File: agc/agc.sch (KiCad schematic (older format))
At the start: 62 parts, among them J5 SIL10, K1 SMD_HDR, K10 SMD_HDR, K11 SMD_HDR, K2 SMD_HDR, K3 SMD_HDR, K4 SMD_HDR, K5 SMD_HDR, K6 SMD_HDR, K7 SMD_HDR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

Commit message: component footprint changes to simplify bom
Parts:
- FID1, FID2, FID3: footprint (none) -> sdtransmitter:FID_1MM
- JP1, JP2, K1, K10, K11, K2, K3, K4, K5, K6, K7, K8, K9: footprint localconn:3-647166-3 -> sdtransmitter:0740991003
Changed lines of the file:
@@
 F 0 "K3" V 850 4550 50  0000 C CNN
 F 1 "SMD_HDR" V 950 4550 40  0000 C CNN
-F 2 "localconn:3-647166-3" H 900 4550 60  0001 C CNN
+F 2 "sdtransmitter:0740991003" H 900 4550 60  0001 C CNN
 F 3 "" H 900 4550 60  0000 C CNN
 	1    900  4550
@@
 F 0 "K5" V 12350 7850 50  0000 C CNN
 F 1 "SMD_HDR" V 12450 7850 40  0000 C CNN
-F 2 "localconn:3-647166-3" H 12400 7850 60  0001 C CNN
+F 2 "sdtransmitter:0740991003" H 12400 7850 60  0001 C CNN
 F 3 "" H 12400 7850 60  0000 C CNN
 	1    12400 7850
@@
 F 0 "K1" V 12350 7400 50  0000 C CNN
 F 1 "SMD_HDR" V 12450 7400 40  0000 C CNN
-F 2 "localconn:3-647166-3" H 12400 7400 60  0001 C CNN
+F 2 "sdtransmitter:0740991003" H 12400 7400 60  0001 C CNN
 F 3 "" H 12400 7400 60  0000 C CNN
 	1    12400 7400
@@
 F 0 "K7" V 10300 3450 50  0000 C CNN
 F 1 "SMD_HDR" V 10400 3450 40  0000 C CNN
-F 2 "localconn:3-647166-3" H 10350 3450 60  0001 C CNN
+F 2 "sdtransmitter:0740991003" H 10350 3450 60  0001 C CNN
 F 3 "" H 10350 3450 60  0000 C CNN
 	1    10350 3450
@@
 F 0 "JP2" H 14150 3200 60  0000 C CNN
 F 1 "SMD_HDR" H 14150 2970 40  0000 C CNN
-F 2 "localconn:3-647166-3" H 14150 3050 60  0001 C CNN
+F 2 "sdtransmitter:0740991003" H 14150 3050 60  0001 C CNN
 F 3 "" H 14150 3050 60  0000 C CNN
 	1    14150 3050
@@
 F 0 "K2" V 12350 8400 50  0000 C CNN
 F 1 "SMD_HDR" V 12450 8400 40  0000 C CNN
-F 2 "localconn:3-647166-3" H 12400 8400 60  0001 C CNN
+F 2 "sdtransmitter:0740991003" H 12400 8400 60  0001 C CNN
 F 3 "" H 12400 8400 60  0000 C CNN
 	1    12400 8400
@@
 F 0 "K4" V 850 3300 50  0000 C CNN
 F 1 "SMD_HDR" V 950 3300 40  0000 C CNN
-F 2 "localconn:3-647166-3" H 900 3300 60  0001 C CNN
+F 2 "sdtransmitter:0740991003" H 900 3300 60  0001 C CNN
 F 3 "" H 900 3300 60  0000 C CNN
 	1    900  3300
@@
 F 0 "K6" V 12350 9050 50  0000 C CNN
 F 1 "SMD_HDR" V 12450 9050 40  0000 C CNN
-F 2 "localconn:3-647166-3" H 12400 9050 60  0001 C CNN
+F 2 "sdtransmitter:0740991003" H 12400 9050 60  0001 C CNN
 F 3 "" H 12400 9050 60  0000 C CNN
 	1    12400 9050
@@
 F 0 "K8" V 15050 7800 50  0000 C CNN
 F 1 "SMD_HDR" V 15150 7800 40  0000 C CNN
-F 2 "localconn:3-647166-3" H 15100 7800 60  0001 C CNN
+F 2 "sdtransmitter:0740991003" H 15100 7800 60  0001 C CNN
 F 3 "" H 15100 7800 60  0000 C CNN
 	1    15100 7800
@@
 F 0 "K9" V 15050 8250 50  0000 C CNN
 F 1 "SMD_HDR" V 15150 8250 40  0000 C CNN
-F 2 "localconn:3-647166-3" H 15100 8250 60  0001 C CNN
+F 2 "sdtransmitter:0740991003" H 15100 8250 60  0001 C CNN
 F 3 "" H 15100 8250 60  0000 C CNN
 	1    15100 8250
@@
 F 0 "JP1" H 8100 2050 60  0000 C CNN
 F 1 "SMD_HDR" H 8100 1820 40  0000 C CNN
-F 2 "localconn:3-647166-3" H 8100 1900 60  0001 C CNN
+F 2 "sdtransmitter:0740991003" H 8100 1900 60  0001 C CNN
 F 3 "" H 8100 1900 60  0000 C CNN
 	1    8100 1900
@@
 F 0 "K10" V 7200 3900 50  0000 C CNN
 F 1 "SMD_HDR" V 7300 3900 40  0000 C CNN
-F 2 "localconn:3-647166-3" H 7250 3900 60  0001 C CNN
+F 2 "sdtransmitter:0740991003" H 7250 3900 60  0001 C CNN
 F 3 "" H 7250 3900 60  0000 C CNN
 	1    7250 3900
@@
 F 0 "K11" V 13250 6650 50  0000 C CNN
 F 1 "SMD_HDR" V 13350 6650 40  0000 C CNN
-F 2 "localconn:3-647166-3" H 13300 6650 60  0001 C CNN
+F 2 "sdtransmitter:0740991003" H 13300 6650 60  0001 C CNN
 F 3 "" H 13300 6650 60  0000 C CNN
 	1    13300 6650
@@
 F 0 "FID1" H 4300 4600 60  0000 C CNN
 F 1 "FIDUCIAL MARKER" H 4600 4700 60  0000 C CNN
-F 2 "" H 4600 4550 60  0000 C CNN
+F 2 "sdtransmitter:FID_1MM" H 4600 4550 60  0001 C CNN
 F 3 "" H 4600 4550 60  0000 C CNN
 	1    4600 4550
@@
 F 0 "FID2" H 5150 4600 60  0000 C CNN
 F 1 "FIDUCIAL MARKER" H 5450 4700 60  0000 C CNN
-F 2 "" H 5450 4550 60  0000 C CNN
+F 2 "sdtransmitter:FID_1MM" H 5450 4550 60  0001 C CNN
 F 3 "" H 5450 4550 60  0000 C CNN
 	1    5450 4550
@@
 F 0 "FID3" H 4300 4900 60  0000 C CNN
 F 1 "FIDUCIAL MARKER" H 4600 5000 60  0000 C CNN
-F 2 "" H 4600 4850 60  0000 C CNN
+F 2 "sdtransmitter:FID_1MM" H 4600 4850 60  0001 C CNN
 F 3 "" H 4600 4850 60  0000 C CNN
 	1    4600 4850

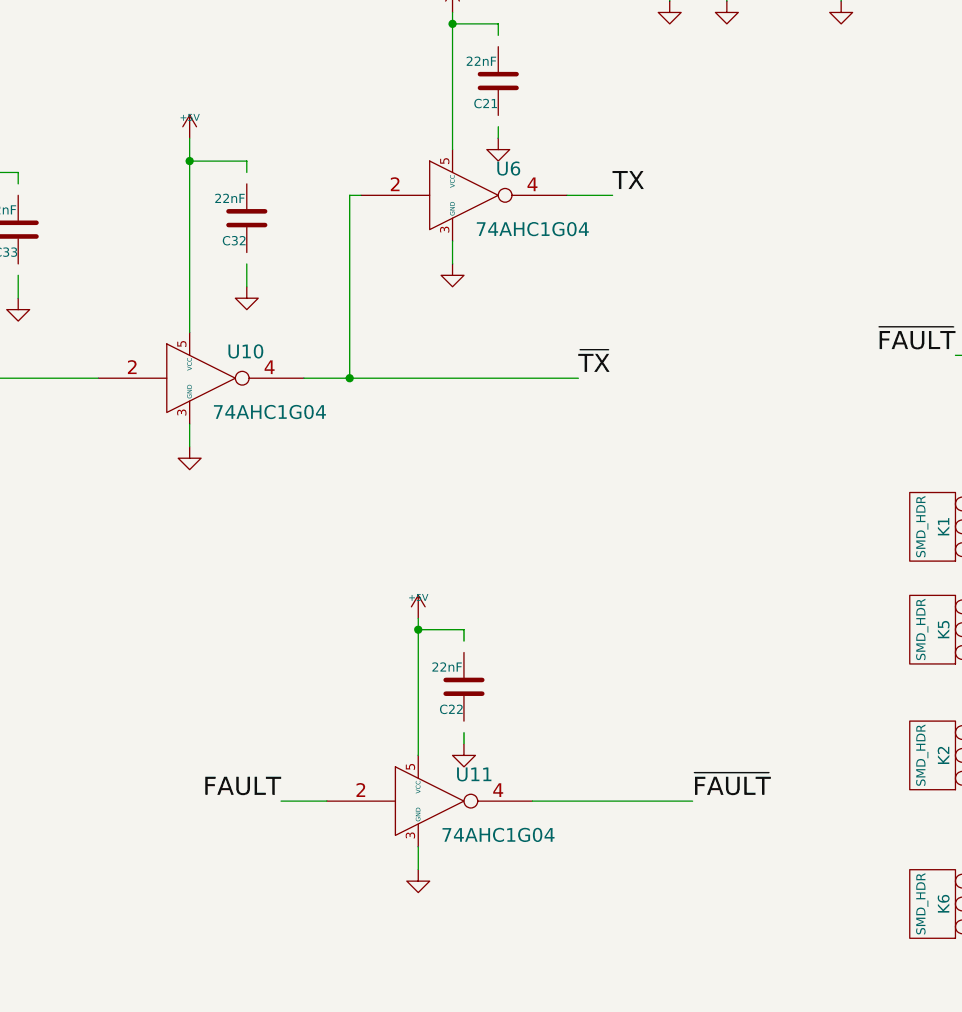
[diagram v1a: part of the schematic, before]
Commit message: added digikey bom for driver amplifier production run
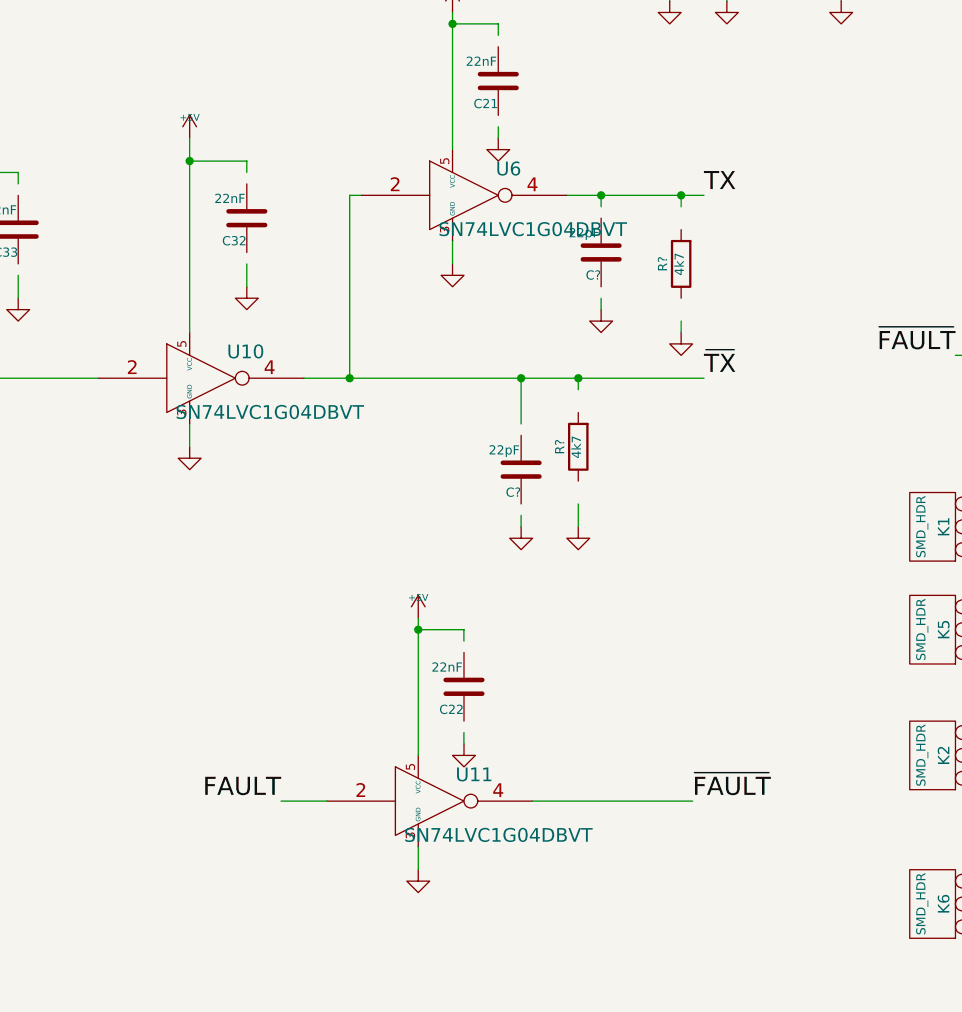
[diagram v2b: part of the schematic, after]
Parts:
- added C? (x2): 22pF, SMD_Packages:SMD-0805, symbol C
- added R? (x2): 4k7, SMD_Packages:SMD-0805, symbol R
- U10, U11, U6: value 74AHC1G04 -> SN74LVC1G04DBVT
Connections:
- wire segments 192 -> 200

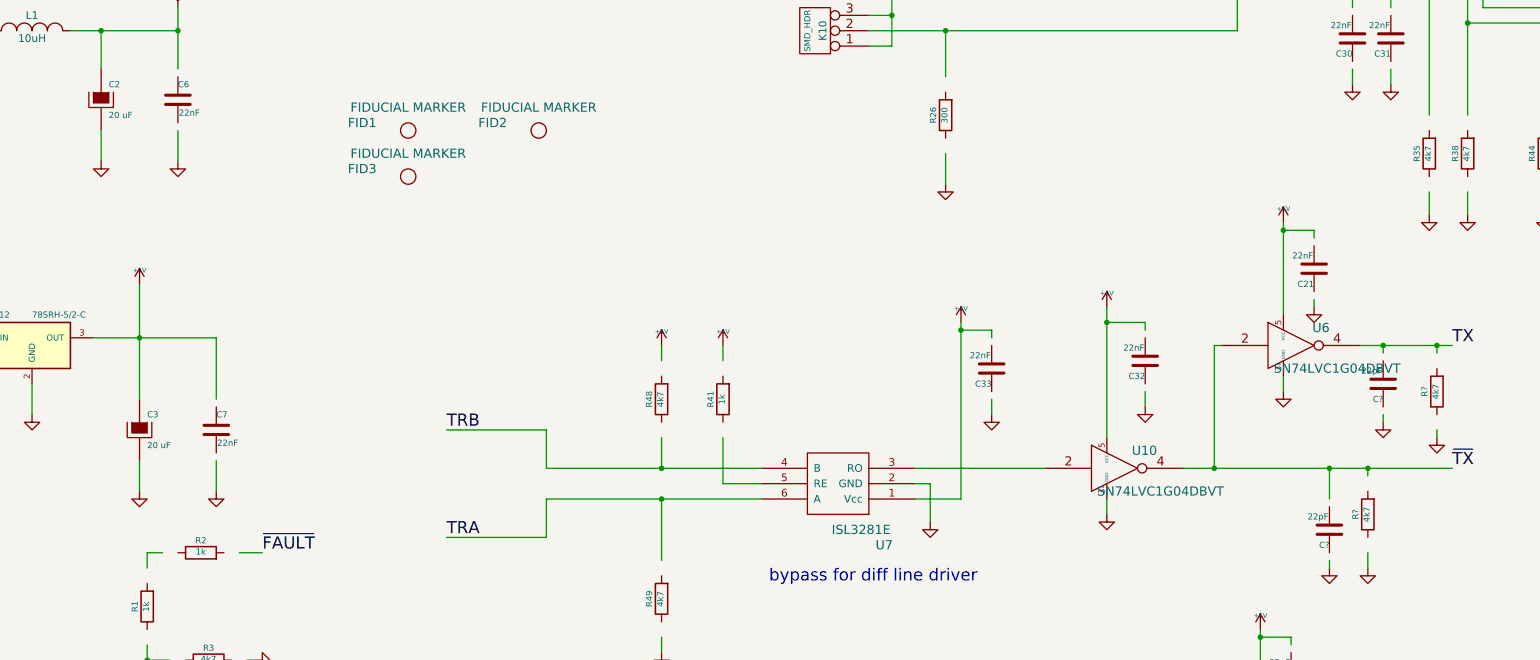
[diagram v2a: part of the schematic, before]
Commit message: added digikey bom for control
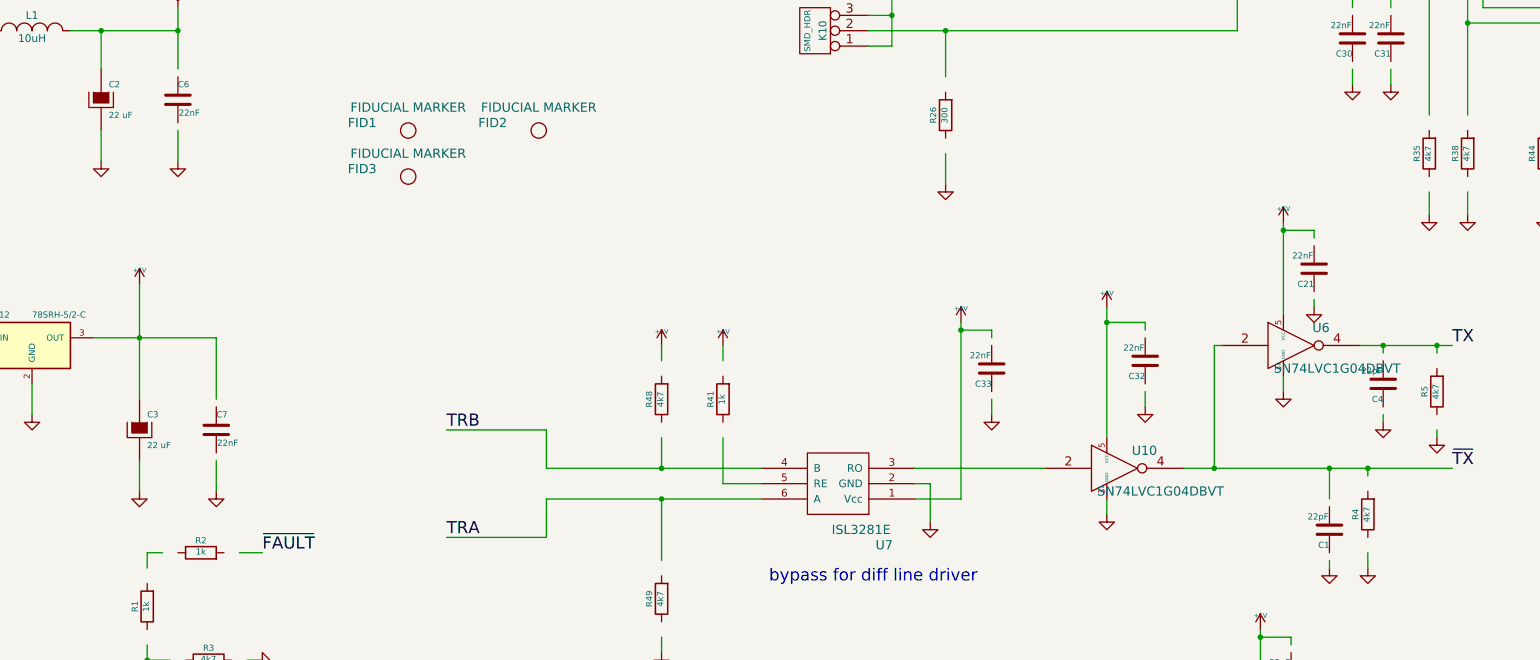
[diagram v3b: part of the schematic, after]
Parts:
- C2, C3: value 20 uF -> 22 uF
- gave numbers to parts that had none: 4

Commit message: added fields for manufacturer/distributor part number to schematic
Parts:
- C1, C4: Dist Name (none) -> DigiKey; Dist PN (none) -> 1276-2607-6-ND; MFG Name (none) -> SAMSUNG ELECTRO-MECHANICS AMERICA, INC (VA); MFG PN (none) -> CL21C220JCANNNC
- C2: Dist Name (none) -> DigiKey; Dist PN (none) -> TDK CORPORATION (VA); MFG Name (none) -> 445-3955-6-ND; MFG PN (none) -> C3225X7R1C226M250AC
- C21: Dist Name (none) -> DigiKey; MFG Name (none) -> MURATA ELECTRONICS (VA); MFG PN (none) -> GRM21BR72A223KA01L
- C22, C28, C29, C30, C31, C32, C33, C6, C7: Dist Name (none) -> DigiKey; Dist PN (none) -> 490-1658-6-ND; MFG Name (none) -> MURATA ELECTRONICS (VA); MFG PN (none) -> GRM21BR72A223KA01L
- C3: Dist Name (none) -> DigiKey; MFG Name (none) -> 445-3955-6-ND; MFG PN (none) -> C3225X7R1C226M250AC
- J5: Dist Name (none) -> DigiKey; Dist PN (none) -> 4610X-1-103LF-ND; MFG Name (none) -> BOURNS INC; MFG PN (none) -> 4610X-101-103LF
- JP1, JP2, K1, K10, K11, K2, K3, K5, K6, K7, K8, K9: Dist Name (none) -> DigiKey; Dist PN (none) -> WM7203-ND; MFG Name (none) -> MOLEX INC; MFG PN (none) -> 740991003
- K4: Dist Name (none) -> Digikey; Dist PN (none) -> WM7203-ND; MFG Name (none) -> MOLEX INC; MFG PN (none) -> 740991003
- L1: Dist Name (none) -> DigiKey; Dist PN (none) -> 587-2409-6-ND; MFG Name (none) -> TAIYO YUDEN (VA); MFG PN (none) -> NRS5020T100MMGJ
- P4: Dist Name (none) -> DigiKey; Dist PN (none) -> 3M11931-ND; MFG Name (none) -> 3M; MFG PN (none) -> 30316-6002HB
- R1, R2, R34, R37, R41, R43: Dist Name (none) -> DigiKey; Dist PN (none) -> P1.00KCDKR-ND; MFG Name (none) -> PANASONIC ELECTRONIC COMPONENTS (VA); MFG PN (none) -> ERJ-6ENF1001V
- R18, R3, R35, R38, R4, R44, R45, R48, R49, R5: Dist Name (none) -> DigiKey; Dist PN (none) -> P4.70KCDKR-ND; MFG Name (none) -> PANASONIC ELECTRONIC COMPONENTS (VA); MFG PN (none) -> ERJ-6ENF4701V
- R23, R33, R36: Dist Name (none) -> DigiKey; Dist PN (none) -> P20.0KCDKR-ND; MFG Name (none) -> PANASONIC ELECTRONIC COMPONENTS (VA); MFG PN (none) -> ERJ-6ENF2002V
- R25, R26: Dist Name (none) -> DigiKey; Dist PN (none) -> P300CDKR-ND; MFG Name (none) -> PANASONIC ELECTRONIC COMPONENTS (VA); MFG PN (none) -> ERJ-6ENF3000V
- R42: Dist Name (none) -> DigiKey; Dist PN (none) -> P100KCDKR-ND; MFG Name (none) -> PANASONIC ELECTRONIC COMPONENTS (VA); MFG PN (none) -> ERJ-6ENF1003V
- U10, U11, U6: Dist Name (none) -> DigiKey; Dist PN (none) -> 296-32289-6-ND; MFG Name (none) -> TEXAS INSTRUMENTS (VA); MFG PN (none) -> SN74LVC1G04DBVT
- U12: Dist Name (none) -> DigiKey; Dist PN (none) -> 811-1119-ND; MFG Name (none) -> MURATA POWER SOLUTIONS INC; MFG PN (none) -> 78SR-5/2-C
- U7: Dist Name (none) -> DigiKey; Dist PN (none) -> ISL3281EIHZ-TDKR-ND; MFG Name (none) -> INTERSIL (VA); MFG PN (none) -> ISL3281EIHZ-T
- U9: Dist Name (none) -> DigiKey; Dist PN (none) -> ADM2914-2ARQZ-ND; MFG Name (none) -> ANALOG DEVICES INC; MFG PN (none) -> ADM2914-2ARQZ

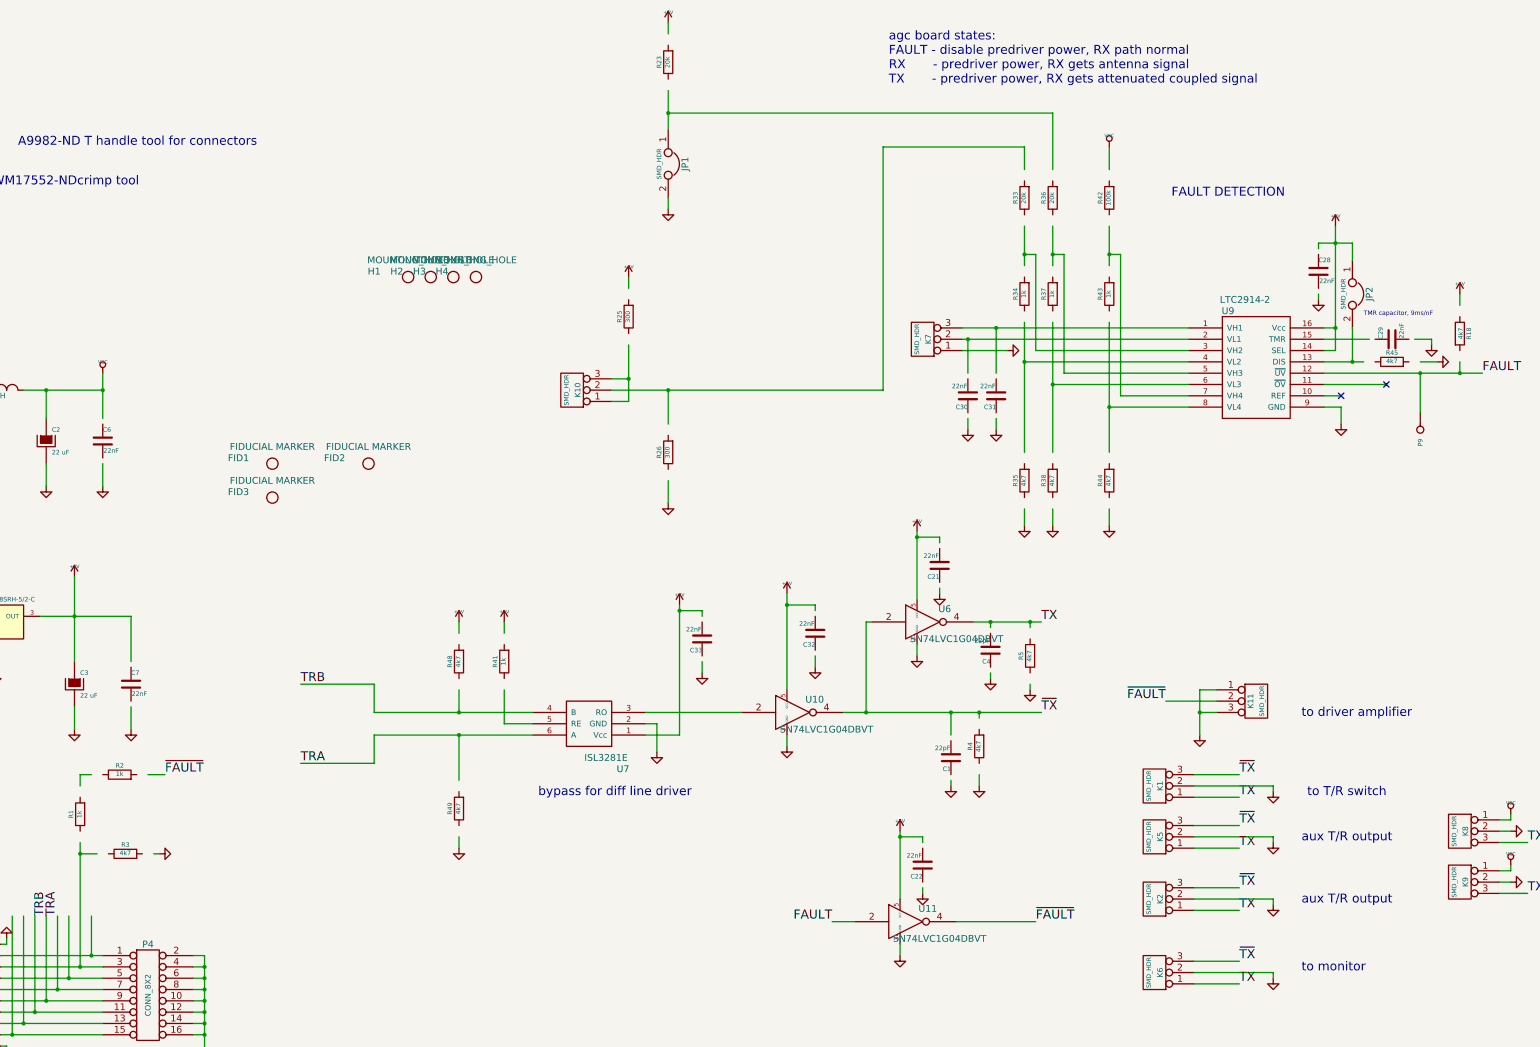
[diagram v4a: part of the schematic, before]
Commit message: updated agc to recent version of kicad - removed vestigial inner layers and fixed schematic for smaller passives
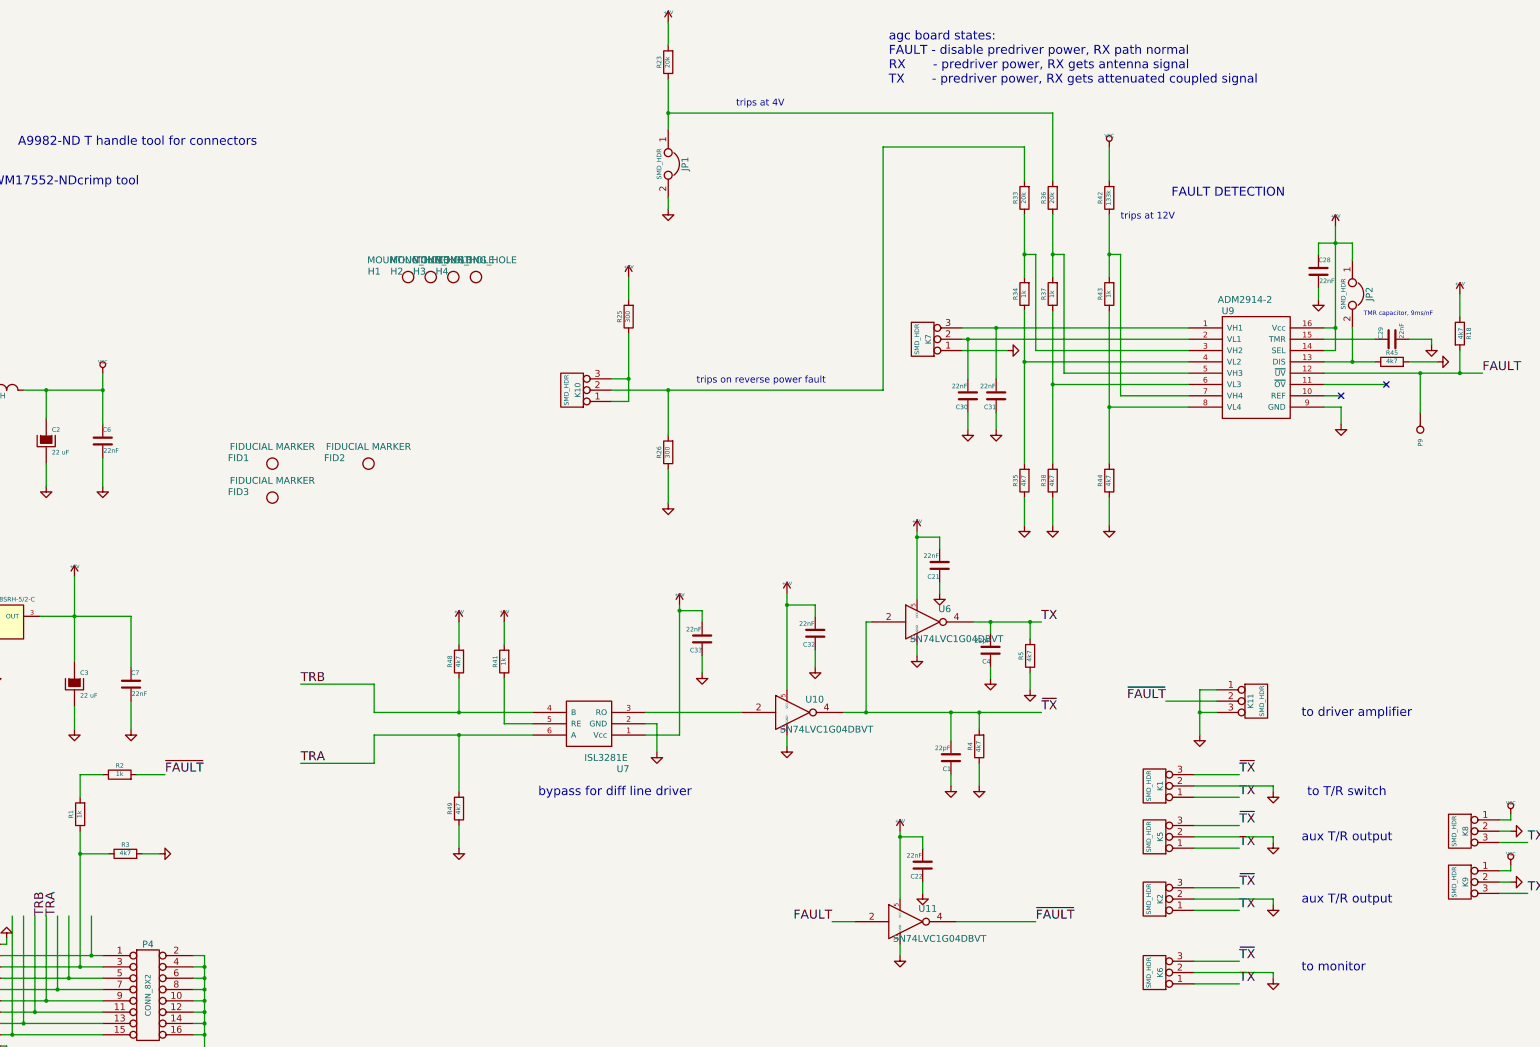
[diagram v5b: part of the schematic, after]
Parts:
- R42: value 100k -> 133k; Dist PN P100KCDKR-ND -> P133KCDKR-ND; MFG PN ERJ-6ENF1003V -> ERJ-6ENF1333V
- U9: value LTC2914-2 -> ADM2914-2
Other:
- note added: "trips at 12V"
- note added: "trips at 4V"
- note added: "trips on reverse power fault\n"
